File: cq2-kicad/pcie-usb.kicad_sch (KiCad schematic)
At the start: 38 parts, among them U13 uPD720202K8, U14 MX25L4006EZNI-12G, X2 24 MHz

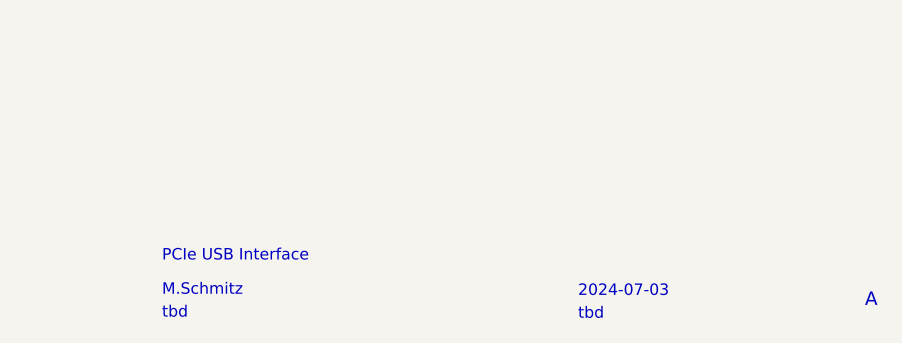
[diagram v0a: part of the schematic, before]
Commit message: drc checked before panalization
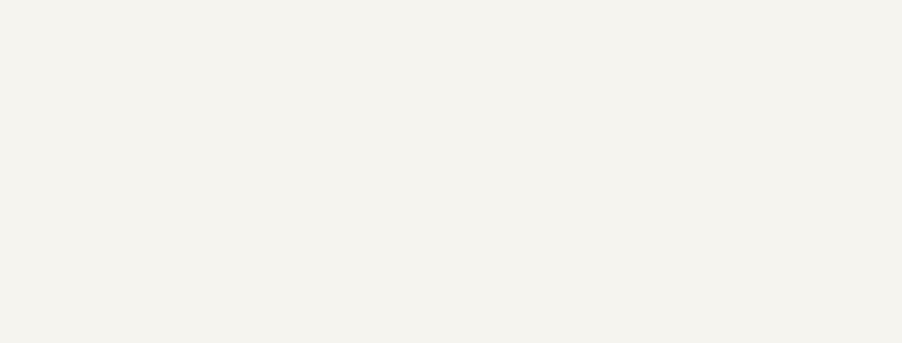
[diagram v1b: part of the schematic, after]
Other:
- note removed: "2024-07-03"
- note removed: "A"
- note removed: "M.Schmitz"
- note removed: "PCIe USB Interface"
- note removed: "tbd"
- title: (none) -> CQ2
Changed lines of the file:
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@@
 	(paper "A4")
 	(title_block
-		(date "2024-07-17")
+		(title "CQ2")
+		(date "2024-07-31")
 		(rev "0")
+		(comment 1 "PCIe USB Interface")
+		(comment 2 "Manfred Schmitz")
+		(comment 3 "tbd")
+		(comment 4 "2024-07-03")
+		(comment 5 "tbd")
+		(comment 6 "A")
 	)
 	(junction
@@
 		)
 	)
-	(text "tbd"
-		(exclude_from_sim no)
-		(at 191.008 193.548 0)
-		(effects
-			(font
-				(size 1.27 1.27)
-			)
-			(justify left bottom)
-		)
-	)
-	(text "A"
-		(exclude_from_sim no)
-		(at 269.113 192.278 0)
-		(effects
-			(font
-				(size 1.4986 1.4986)
-			)
-			(justify left bottom)
-		)
-	)
 	(text "Programmed part:	660.45.00004.50.40\nUnprogrammed part:	660.45.00004.50.2 "
 		(exclude_from_sim no)
@@
 		)
 	)
-	(text "2024-07-03"
-		(exclude_from_sim no)
-		(at 237.236 191.135 0)
-		(effects
-			(font
-				(size 1.27 1.27)
-			)
-			(justify left bottom)
-		)
-	)
-	(text "PCIe USB Interface"
-		(exclude_from_sim no)
-		(at 191.008 187.198 0)
-		(effects
-			(font
-				(size 1.27 1.27)
-			)
-			(justify left bottom)
-		)
-	)
-	(text "tbd"
-		(exclude_from_sim no)
-		(at 237.236 193.675 0)
-		(effects
-			(font
-				(size 1.27 1.27)
-			)
-			(justify left bottom)
-		)
-	)
-	(text "M.Schmitz"
-		(exclude_from_sim no)
-		(at 191.008 191.008 0)
-		(effects
-			(font
-				(size 1.27 1.27)
-			)
-			(justify left bottom)
-		)
-	)
 	(label "+1V"
 		(at 267.97 29.21 180)
@@
 		)
 	)
+	(netclass_flag ""
+		(length 1.28)
+		(shape round)
+		(at 99.06 82.55 0)
+		(effects
+			(font
+				(size 1.27 1.27)
+			)
+			(justify left bottom)
+		)
+		(property "Netclass" "PCIE"
+			(at 99.568 81.28 0)
+			(effects
+				(font
+					(size 1.27 1.27)
+					(italic yes)
+				)
+				(justify left)
+			)
+		)
+	)
+	(netclass_flag ""
+		(length 1.28)
+		(shape round)
+		(at 99.06 85.09 0)
+		(effects
+			(font
+				(size 1.27 1.27)
+			)
+			(justify left bottom)
+		)
+		(property "Netclass" "PCIE"
+			(at 99.568 83.82 0)
+			(effects
+				(font
+					(size 1.27 1.27)
+					(italic yes)
+				)
+				(justify left)
+			)
+		)
+	)
+	(netclass_flag ""
+		(length 2.54)
+		(shape round)
+		(at 129.54 29.21 0)
+		(fields_autoplaced yes)
+		(effects
+			(font
+				(size 1.27 1.27)
+			)
+			(justify left bottom)
+		)
+		(property "Netclass" "PWR"
+			(at 130.1496 26.67 0)
+			(effects
+				(font
+					(size 1.27 1.27)
+					(italic yes)
+				)
+				(justify left)
+			)
+		)
+	)
 	(symbol
 		(lib_id "ci4rail-database:capacitors/93")
@@
 			)
 		)
-		(property "Lifecyle" ""
-			(at 58.42 74.93 0)
-			(effects
-				(font
-					(size 1.27 1.27)
-				)
-				(hide yes)
-			)
-		)
 		(pin "1"
 		)
@@
 			(at 58.42 80.01 0)
 			(effects
-				(font
-					(size 1.27 1.27)
-				)
-				(hide yes)
-			)
-		)
-		(property "Lifecyle" ""
-			(at 58.42 80.01 0)
-			(effects

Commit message: Production documents created
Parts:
- U13: Lifecycle review pending CQ2 -> ERP1 pending CQ2; Outline (none) -> SMT QFN-48
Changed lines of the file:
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@@
 	(title_block
 		(title "CQ2")
-		(date "2024-07-31")
+		(date "2024-08-03")
 		(rev "0")
 		(comment 1 "PCIe USB Interface")
@@
 			)
 		)
-		(property "Lifecycle" "review pending CQ2"
+		(property "Lifecycle" "ERP1 pending CQ2"
 			(at 152.4 97.79 0)
 			(effects
@@
 			)
 		)
-		(property "Outline" ""
+		(property "Outline" "SMT QFN-48"
 			(at 152.4 97.79 0)
 			(effects
